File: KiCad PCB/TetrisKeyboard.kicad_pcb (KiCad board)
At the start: 2 copper layers, 100 x 100 mm, 31 parts, among them SW1 CherryMX_1.00u_KailhSocket, SW10 CherryMX_1.00u_KailhSocket, SW2 CherryMX_1.00u_KailhSocket, SW3 CherryMX_1.00u_KailhSocket, SW4 CherryMX_1.00u_KailhSocket, SW5 CherryMX_1.00u_KailhSocket, SW6 CherryMX_1.00u_KailhSocket, SW7 CherryMX_1.00u_KailhSocket, SW8 CherryMX_1.00u_KailhSocket, SW9 CherryMX_1.00u_KailhSocket

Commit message: Update socket footprint and add versioning
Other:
- board text added: "22/09/24"
- board text added: "Tetris Keyboard v0.0.2"
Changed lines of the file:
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@@
 		)
 		(pad "" np_thru_hole circle
+			(at -5.08 0)
+			(size 1.7 1.7)
+			(drill 1.7)
+			(layers "*.Cu" "*.Mask")
+		)
+		(pad "" np_thru_hole circle
 			(at -3.81 -2.54)
 			(size 3 3)
@@
 			(layers "*.Cu" "*.Mask")
 		)
+		(pad "" np_thru_hole circle
+			(at 5.08 0)
+			(size 1.7 1.7)
+			(drill 1.7)
+			(layers "*.Cu" "*.Mask")
+		)
 		(pad "1" smd rect
 			(at -7.41 -2.54)
@@
 		)
 		(pad "" np_thru_hole circle
+			(at -5.08 0)
+			(size 1.7 1.7)
+			(drill 1.7)
+			(layers "*.Cu" "*.Mask")
+		)
+		(pad "" np_thru_hole circle
 			(at -3.81 -2.54)
 			(size 3 3)
@@
 			(layers "*.Cu" "*.Mask")
 		)
+		(pad "" np_thru_hole circle
+			(at 5.08 0)
+			(size 1.7 1.7)
+			(drill 1.7)
+			(layers "*.Cu" "*.Mask")
+		)
 		(pad "1" smd rect
 			(at -7.41 -2.54)
@@
 		)
 		(pad "" np_thru_hole circle
+			(at -5.08 0)
+			(size 1.7 1.7)
+			(drill 1.7)
+			(layers "*.Cu" "*.Mask")
+		)
+		(pad "" np_thru_hole circle
 			(at -3.81 -2.54)
 			(size 3 3)
@@
 			(layers "*.Cu" "*.Mask")
 		)
+		(pad "" np_thru_hole circle
+			(at 5.08 0)
+			(size 1.7 1.7)
+			(drill 1.7)
+			(layers "*.Cu" "*.Mask")
+		)
 		(pad "1" smd rect
 			(at -7.41 -2.54)
@@
 		)
 		(pad "" np_thru_hole circle
+			(at -5.08 0)
+			(size 1.7 1.7)
+			(drill 1.7)
+			(layers "*.Cu" "*.Mask")
+		)
+		(pad "" np_thru_hole circle
 			(at -3.81 -2.54)
 			(size 3 3)
@@
 			(layers "*.Cu" "*.Mask")
 		)
+		(pad "" np_thru_hole circle
+			(at 5.08 0)
+			(size 1.7 1.7)
+			(drill 1.7)
+			(layers "*.Cu" "*.Mask")
+		)
 		(pad "1" smd rect
 			(at -7.41 -2.54)
@@
 		)
 		(pad "" np_thru_hole circle
+			(at -5.08 0)
+			(size 1.7 1.7)
+			(drill 1.7)
+			(layers "*.Cu" "*.Mask")
+		)
+		(pad "" np_thru_hole circle
 			(at -3.81 -2.54)
 			(size 3 3)
@@
 			(layers "*.Cu" "*.Mask")
 		)
+		(pad "" np_thru_hole circle
+			(at 5.08 0)
+			(size 1.7 1.7)
+			(drill 1.7)
+			(layers "*.Cu" "*.Mask")
+		)
 		(pad "1" smd rect
 			(at -7.41 -2.54)
@@
 		)
 		(pad "" np_thru_hole circle
+			(at -5.08 0)
+			(size 1.7 1.7)
+			(drill 1.7)
+			(layers "*.Cu" "*.Mask")
+		)
+		(pad "" np_thru_hole circle
 			(at -3.81 -2.54)
 			(size 3 3)
@@
 			(layers "*.Cu" "*.Mask")
 		)
+		(pad "" np_thru_hole circle
+			(at 5.08 0)
+			(size 1.7 1.7)
+			(drill 1.7)
+			(layers "*.Cu" "*.Mask")
+		)
 		(pad "1" smd rect
 			(at -7.41 -2.54)
@@
 		)
 		(pad "" np_thru_hole circle
+			(at -5.08 0)
+			(size 1.7 1.7)
+			(drill 1.7)
+			(layers "*.Cu" "*.Mask")
+		)
+		(pad "" np_thru_hole circle
 			(at -3.81 -2.54)
 			(size 3 3)
@@
 			(layers "*.Cu" "*.Mask")
 		)
+		(pad "" np_thru_hole circle
+			(at 5.08 0)
+			(size 1.7 1.7)
+			(drill 1.7)
+			(layers "*.Cu" "*.Mask")
+		)
 		(pad "1" smd rect
 			(at -7.41 -2.54)
@@
 		)
 		(pad "" np_thru_hole circle
+			(at -5.08 0)
+			(size 1.7 1.7)
+			(drill 1.7)
+			(layers "*.Cu" "*.Mask")
+		)
+		(pad "" np_thru_hole circle
 			(at -3.81 -2.54)
 			(size 3 3)
@@
 			(layers "*.Cu" "*.Mask")
 		)
+		(pad "" np_thru_hole circle
+			(at 5.08 0)
+			(size 1.7 1.7)
+			(drill 1.7)
+			(layers "*.Cu" "*.Mask")
+		)
 		(pad "1" smd rect
 			(at -7.41 -2.54)
@@
 		)
 		(pad "" np_thru_hole circle
+			(at -5.08 0)
+			(size 1.7 1.7)
+			(drill 1.7)
+			(layers "*.Cu" "*.Mask")
+		)
+		(pad "" np_thru_hole circle
 			(at -3.81 -2.54)
 			(size 3 3)
@@
 			(layers "*.Cu" "*.Mask")
 		)
+		(pad "" np_thru_hole circle
+			(at 5.08 0)
+			(size 1.7 1.7)
+			(drill 1.7)
+			(layers "*.Cu" "*.Mask")
+		)
 		(pad "1" smd rect
 			(at -7.41 -2.54)
@@
 		)
 		(pad "" np_thru_hole circle
+			(at -5.08 0)
+			(size 1.7 1.7)
+			(drill 1.7)
+			(layers "*.Cu" "*.Mask")
+		)
+		(pad "" np_thru_hole circle
 			(at -3.81 -2.54)
 			(size 3 3)
@@
 			(layers "*.Cu" "*.Mask")
 		)
+		(pad "" np_thru_hole circle
+			(at 5.08 0)
+			(size 1.7 1.7)
+			(drill 1.7)
+			(layers "*.Cu" "*.Mask")
+		)
 		(pad "1" smd rect
 			(at -7.41 -2.54)
@@
 		(layer "Edge.Cuts")
 	)
+	(gr_text "22/09/24"
+		(at 206.9 193.9 0)
+		(layer "Edge.Cuts")
+		(effects
+			(font
+				(size 1 1)
+				(thickness 0.15)
+			)
+			(justify left bottom)
+		)
+	)
+	(gr_text "Tetris Keyboard v0.0.2"
+		(at 186.7 189.9 0)
+		(layer "Edge.Cuts")
+		(effects
+			(font
+				(size 1 1)
+				(thickness 0.15)
+			)
+			(justify left bottom)
+		)
+	)
 	(segment

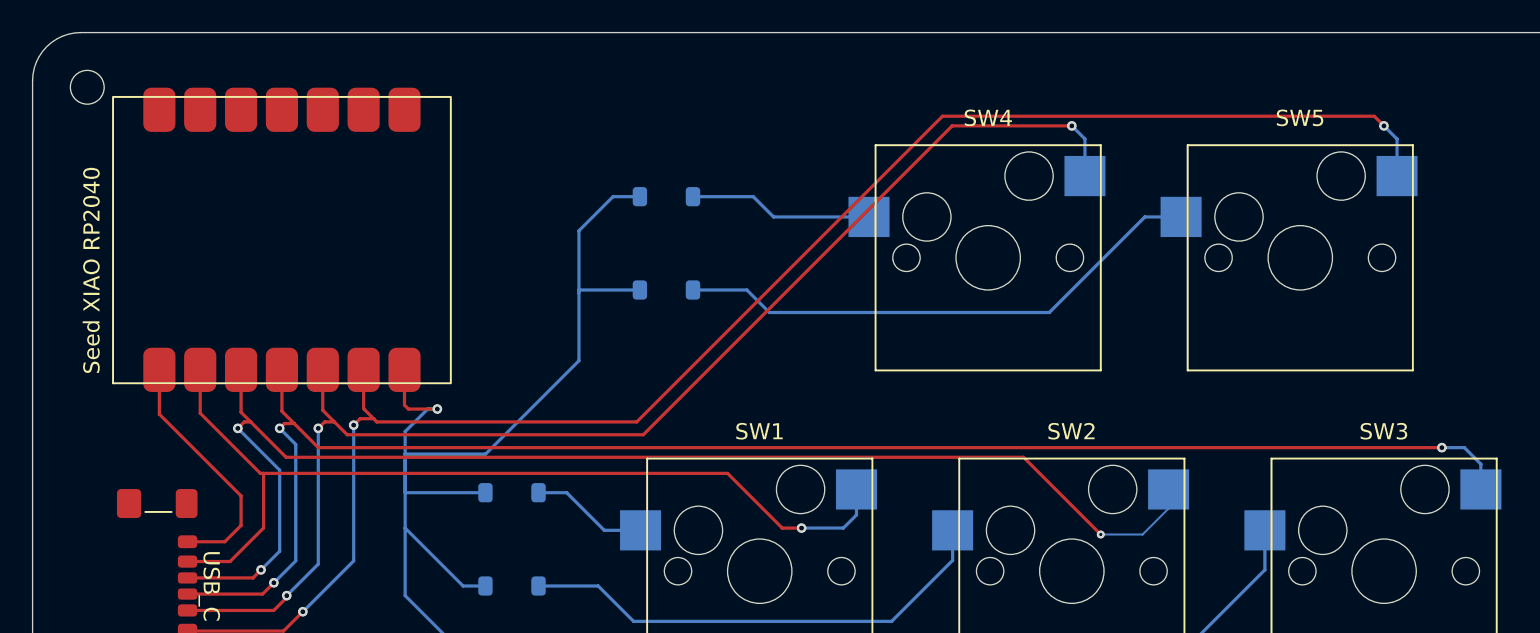
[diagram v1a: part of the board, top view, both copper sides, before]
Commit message: Update TetrisKeyboard.kicad_pcb
Fix RP2040 covering mounting hole
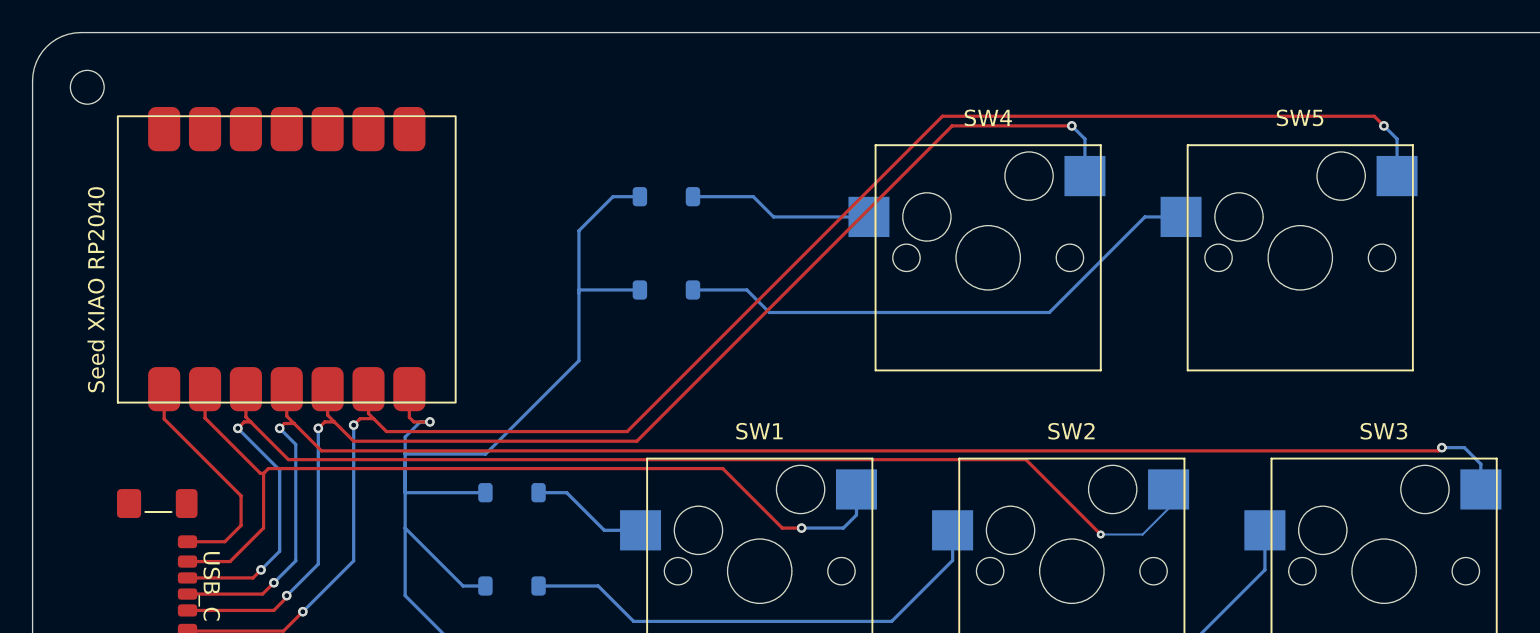
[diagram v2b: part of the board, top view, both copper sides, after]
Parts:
- moved Seed XIAO RP2040 1.24 mm to (44.9, 54.8)
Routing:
- net Row1: track 200.1 -> 198.0 mm
- net Row2: track 15.5 -> 14.2 mm
- net Col2: track 81.4 -> 80.1 mm
- net Col3: track 97.3 -> 96.1 mm
- net Col1: track 57.4 -> 56.3 mm
- net Col4: track 80.2 -> 79.2 mm
- net Col5: track 99.8 -> 98.9 mm
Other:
- board text added: "Tetris Keyboard v0.0.3"
- board text removed: "Tetris Keyboard v0.0.2"

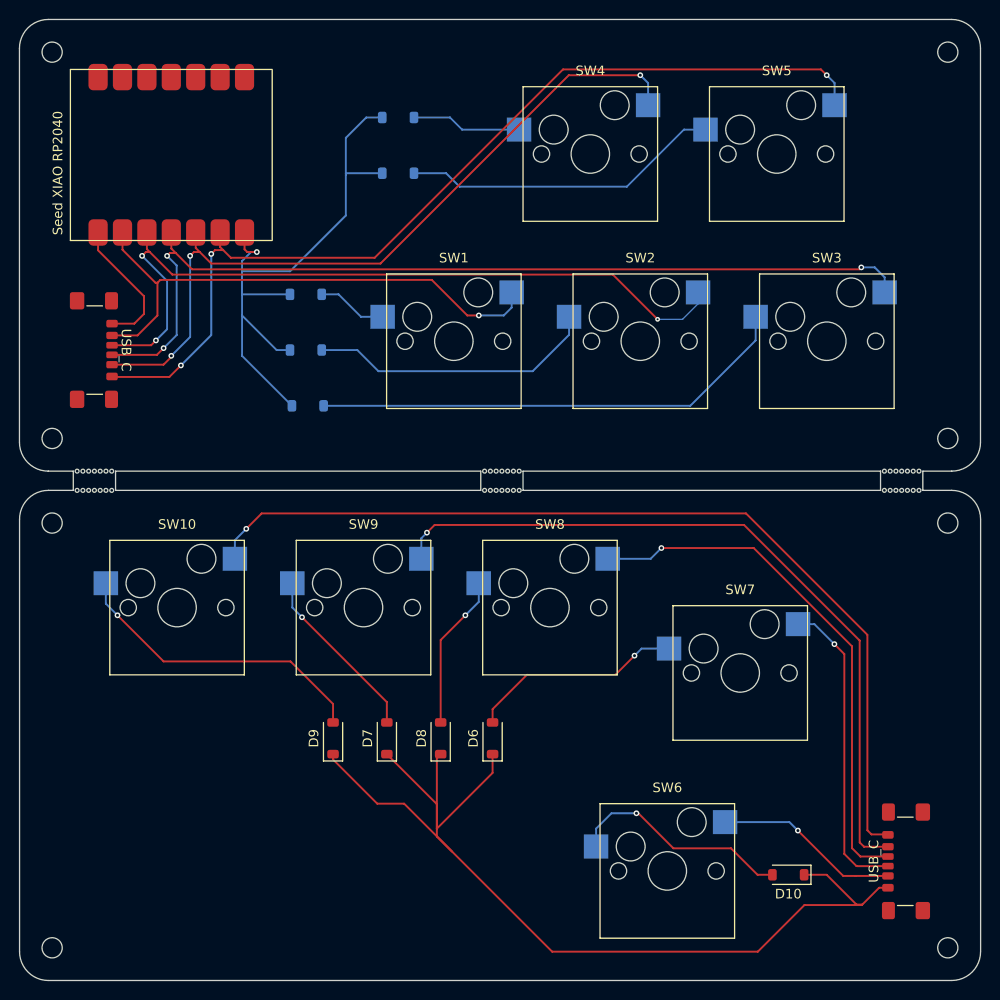
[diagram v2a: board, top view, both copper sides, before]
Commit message: Update TetrisKeyboard.kicad_pcb
Fix text on wrong layer and slight movement of keys
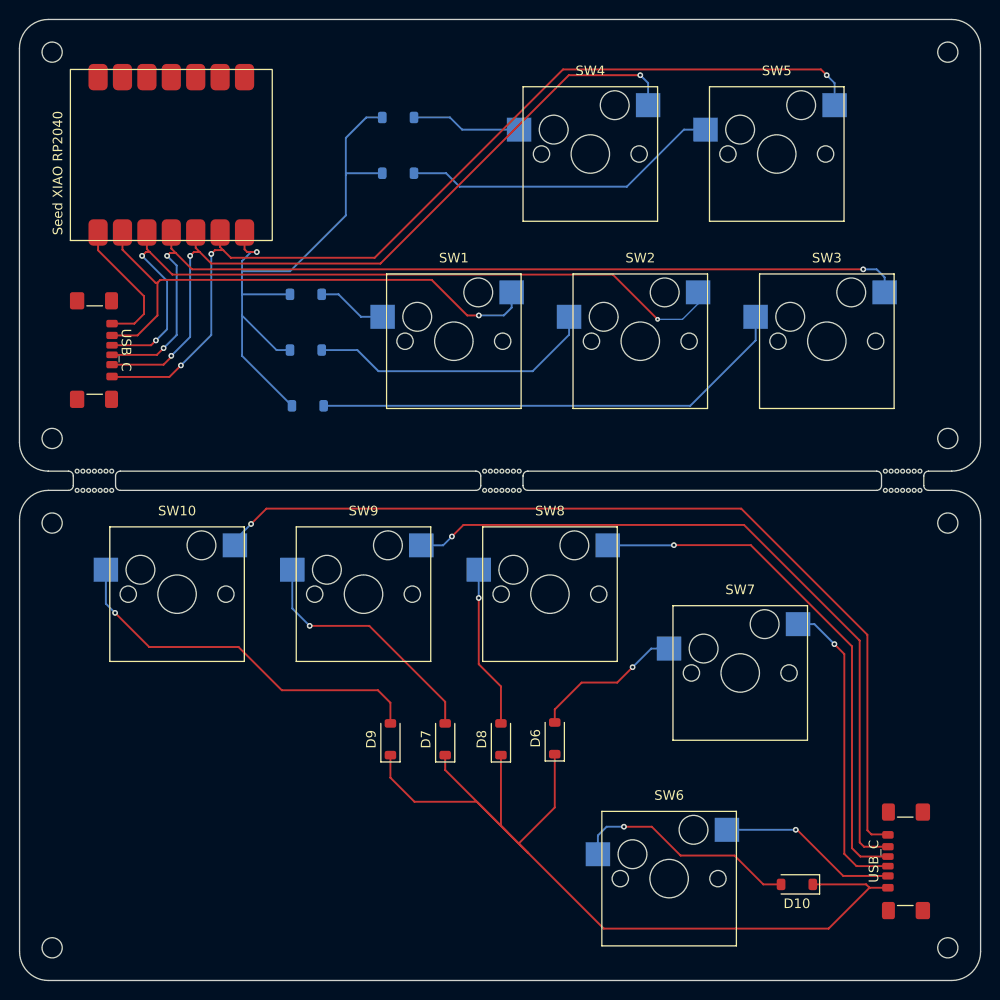
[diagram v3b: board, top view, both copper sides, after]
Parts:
- moved D6 6.47 mm to (74.3, 106.6)
- moved D8 6.27 mm to (68.7, 106.7)
- moved D7 6.07 mm to (62.9, 106.7)
- moved D9 5.97 mm to (57.2, 106.7)
- moved SW10 1.40 mm to (35.0, 91.6)
- moved SW8 1.40 mm to (73.8, 91.6)
- moved SW9 1.40 mm to (54.4, 91.6)
- moved D10 1.35 mm to (99.5, 121.8)
- moved SW6 0.82 mm to (86.2, 121.2)
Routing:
- net Row2-B: track 220.3 -> 225.2 mm
- net Col4-B: track 77.4 -> 75.6 mm
- net Col5-B: track 96.8 -> 95.2 mm
- net Col2: track 80.1 -> 78.9 mm
- net Col1-B: track 19.3 -> 18.7 mm
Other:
- outline, holes or cut-outs redrawn
- board text added: "Tetris Keyboard"
- board text removed: "Tetris Keyboard v0.0.3"

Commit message: Update Kicad
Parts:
- moved USB_C 0.21 mm to (112.0, 119.2)
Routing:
- net Col2: track 78.9 -> 80.2 mm
- net Col5-B: track 95.2 -> 94.6 mm
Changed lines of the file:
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@@
 	(footprint "Connector_USB:USB_C_Receptacle_GCT_USB4135-GF-A_6P_TopMnt_Horizontal"
 		(layer "F.Cu")
-		(at 112 119.4 90)
+		(at 112.05 119.2 90)
 		(descr "USB Type C Receptacle, GCT, power-only, 6P, top mounted, horizontal, 3A: https://gct.co/files/drawings/usb4135.pdf")
 		(tags "USB C Type-C Receptacle SMD USB Power-only Charging-only 6P 6C USB4135-GF-A")
@@
 	)
 	(segment
-		(start 38.56 56.2)
+		(start 38.63 56.13)
 		(end 38.96 55.8)
 		(width 0.2)
@@
 	)
 	(via
-		(at 38.56 56.2)
+		(at 38.63 56.13)
 		(size 0.6)
 		(drill 0.3)
@@
 	)
 	(segment
+		(start 38.63 56.13)
+		(end 38.56 56.2)
+		(width 0.2)
+		(layer "B.Cu")
+		(net 1)
+	)
+	(segment
+		(start 38.56 64.64)
+		(end 35.4 67.8)
+		(width 0.2)
+		(layer "B.Cu")
+		(net 1)
+	)
+	(segment
 		(start 103.415 40.72)
 		(end 103.415 38.415)
@@
 	)
 	(segment
-		(start 38.56 64.64)
-		(end 35.4 67.8)
-		(width 0.2)
-		(layer "B.Cu")
-		(net 1)
-	)
-	(segment
 		(start 34.455736 66.855736)
 		(end 33.591472 67.72)
@@
 	)
 	(segment
-		(start 33.96 59)
-		(end 31.36 56.4)
+		(start 87.9 63)
+		(end 85 63)
 		(width 0.2)
 		(layer "B.Cu")
@@
 	)
 	(segment
-		(start 87.6 63)
-		(end 89.215 61.385)
-		(width 0.127)
+		(start 33.96 59)
+		(end 31.36 56.4)
+		(width 0.2)
 		(layer "B.Cu")
 		(net 3)
@@
 	)
 	(segment
+		(start 89.215 61.685)
+		(end 87.9 63)
+		(width 0.2)
+		(layer "B.Cu")
+		(net 3)
+	)
+	(segment
 		(start 32.8 65.2)
 		(end 33.96 64.04)
@@
 	)
 	(segment
-		(start 85 63)
-		(end 87.6 63)
-		(width 0.127)
+		(start 89.215 60.2)
+		(end 89.215 61.685)
+		(width 0.2)
 		(layer "B.Cu")
 		(net 3)
@@
 	)
 	(segment
-		(start 42.7 84.3)
-		(end 44.3 82.7)
+		(start 106.83 95.83)
+		(end 106.83 115.53)
 		(width 0.2)
 		(layer "F.Cu")
@@
 	)
 	(segment
-		(start 93.7 82.7)
-		(end 106.83 95.83)
+		(start 44.3 82.7)
+		(end 93.7 82.7)
 		(width 0.2)
 		(layer "F.Cu")
@@
 	)
 	(segment
-		(start 107.26 116.6)
-		(end 108.9175 116.6)
+		(start 93.7 82.7)
+		(end 106.83 95.83)
 		(width 0.2)
 		(layer "F.Cu")
@@
 	)
 	(segment
-		(start 44.3 82.7)
-		(end 93.7 82.7)
+		(start 107.75 116.45)
+		(end 108.7675 116.45)
 		(width 0.2)
 		(layer "F.Cu")
@@
 	)
 	(segment
-		(start 106.83 116.17)
-		(end 107.26 116.6)
+		(start 106.83 115.53)
+		(end 107.75 116.45)
 		(width 0.2)
 		(layer "F.Cu")
@@
 	)
 	(segment
-		(start 106.83 95.83)
-		(end 106.83 116.17)
+		(start 42.7 84.3)
+		(end 44.3 82.7)
 		(width 0.2)
 		(layer "F.Cu")
@@
 	)
 	(segment
-		(start 106.48 117.88)
-		(end 108.9675 117.88)
+		(start 106.03 96.43)
+		(end 106.03 117.03)
 		(width 0.2)
 		(layer "F.Cu")
@@
 	)
 	(segment
-		(start 106.03 117.43)
-		(end 106.48 117.88)
+		(start 94 84.4)
+		(end 106.03 96.43)
 		(width 0.2)
 		(layer "F.Cu")
@@
 	)
 	(segment
-		(start 63.6 85.6)
-		(end 64.8 84.4)
+		(start 106.68 117.68)
+		(end 109.0175 117.68)
 		(width 0.2)
 		(layer "F.Cu")
@@
 	)
 	(segment
-		(start 64.8 84.4)
-		(end 94 84.4)
+		(start 106.03 117.03)
+		(end 106.68 117.68)
 		(width 0.2)
 		(layer "F.Cu")
@@
 	)
 	(segment
-		(start 106.03 96.43)
-		(end 106.03 117.43)
+		(start 63.6 85.6)
+		(end 64.8 84.4)
 		(width 0.2)
 		(layer "F.Cu")
@@
 	)
 	(segment
-		(start 94 84.4)
-		(end 106.03 96.43)
+		(start 64.8 84.4)
+		(end 94 84.4)
 		(width 0.2)
 		(layer "F.Cu")
@@
 	)
 	(segment
-		(start 86.7 86.5)
-		(end 94.7 86.5)
+		(start 94.7 86.5)
+		(end 105.23 97.03)
 		(width 0.2)
 		(layer "F.Cu")
@@
 	)
 	(segment
-		(start 105.23 118.03)
-		(end 106.1 118.9)
+		(start 86.7 86.5)
+		(end 94.7 86.5)
 		(width 0.2)
 		(layer "F.Cu")
@@
 	)
 	(segment
-		(start 105.23 97.03)
-		(end 105.23 118.03)
+		(start 106 118.7)
+		(end 109.0175 118.7)
 		(width 0.2)
 		(layer "F.Cu")
@@
 	)
 	(segment
-		(start 94.7 86.5)
-		(end 105.23 97.03)
+		(start 105.23 117.93)
+		(end 106 118.7)
 		(width 0.2)
 		(layer "F.Cu")
@@
 	)
 	(segment
-		(start 106.1 118.9)
-		(end 108.9675 118.9)
+		(start 105.23 97.03)
+		(end 105.23 117.93)
 		(width 0.2)
 		(layer "F.Cu")
@@
 	)
 	(segment
-		(start 104.32 120.92)
-		(end 108.9675 120.92)
+		(start 99.52 116.12)
+		(end 104.12 120.72)
 		(width 0.2)
 		(layer "F.Cu")
@@
 	)
 	(segment
-		(start 99.52 116.12)
-		(end 104.32 120.92)
+		(start 104.12 120.72)
+		(end 109.0175 120.72)
 		(width 0.2)
 		(layer "F.Cu")
@@
 	)
 	(segment
-		(start 104.43 97.83)
-		(end 104.43 118.63)
+		(start 104.43 118.63)
+		(end 105.5 119.7)
 		(width 0.2)
 		(layer "F.Cu")
@@
 	)
 	(segment
-		(start 105.7 119.9)
-		(end 108.9675 119.9)
+		(start 105.5 119.7)
+		(end 109.0175 119.7)
 		(width 0.2)
 		(layer "F.Cu")
@@
 	)
 	(segment
-		(start 104.43 118.63)
-		(end 105.7 119.9)
+		(start 104.43 97.83)
+		(end 104.43 118.63)
 		(width 0.2)
 		(layer "F.Cu")
@@
 	)
 	(segment
-		(start 106.7 121.8)
-		(end 107.05 122.15)
-		(width 0.2)
-		(layer "F.Cu")
-		(net 13)
-	)
-	(segment
 		(start 57.2 102.9)
 		(end 57.2 105.05)
@@
 	)
 	(segment
-		(start 107.05 122.15)
-		(end 108.9675 122.15)
-		(width 0.2)
-		(layer "F.Cu")
-		(net 13)
-	)
-	(segment
 		(start 74.3 108.25)
 		(end 74.3 113.8)
@@
 	(segment
 		(start 101.15 121.8)
-		(end 106.7 121.8)
+		(end 107.1 121.8)
 		(width 0.2)
 		(layer "F.Cu")
@@
 	)
 	(segment
+		(start 107.25 121.95)
+		(end 109.0175 121.95)
+		(width 0.2)
+		(layer "F.Cu")
+		(net 13)
+	)
+	(segment
+		(start 107.1 121.8)
+		(end 107.25 121.95)
+		(width 0.2)
+		(layer "F.Cu")
+		(net 13)
+	)
+	(segment
 		(start 79.4 126.4)
 		(end 102.8 126.4)
@@
 		(width 0.2)
 		(layer "F.Cu")
+		(net 13)
+	)
+	(segment
+		(start 107.05 122.15)
+		(end 107.25 121.95)
+		(width 0.2)
+		(layer "F.Cu")
